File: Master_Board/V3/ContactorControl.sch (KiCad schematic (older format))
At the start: 28 parts, among them J701 649002227222, J702 649004227222, J703 649004227222, J704 649004227222, Q701 BC849BLT1G, Q702 BC849BLT1G, Q703 BC849BLT1G, Q704 BC849BLT1G

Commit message: Rooting Master V3
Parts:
- removed J701: 649002227222, Connectors:649002227222, symbol 649002227222
- removed R705, R706, R707, R708: RC0805FR-071K1L, Resistors:R0805, symbol RC0805FR-071K1L
- removed R?: RC0805JR-076K8L, Resistors:R0805, symbol RC0805JR-076K8L
- removed U?: CPC1117NTR, IC:4-SOP, symbol CPC1117NTR
- added J704: 649002227222, Connectors:649002227222, symbol 649002227222
- added R705, R706, R707, R708: RC0805JR-072K2L, Resistors:R0805, symbol RC0805JR-072K2L
- added R712: RC0805JR-076K8L, Resistors:R0805, symbol RC0805JR-076K8L
- added U701: CPC1117NTR, IC:4-SOP, symbol CPC1117NTR
- renumbered J702 to J701, J703 to J702, J704 to J703
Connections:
- net 12V_Contactor: now also J704.2; no longer RL701.7, RL701.8
- net 3.3V: now also U701.4 (DC+)
- net DGND: now also R712.2
- net Kill_Switch_State: now also U701.3 (DC-)
- net at Q701.3 (C): now also R705.1
- net at RL701.3: now also R705.2
- net at RL702.3: now also R706.2
- net at RL703.3: now also R707.2
- net at RL704.3: now also R708.2
- net at Q702.3 (C): now also R706.1
- net at Q703.3 (C): now also R707.1
- net at Q704.3 (C): now also R708.1
- new net: R712.1, U701.2 (C-)
- new net 12V_Protected: J704.1, RL701.7, RL701.8, U701.1 (A+)
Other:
- note removed: "Bouton d'arrêt d'urgence"
- moved on the sheet: D701, D702, D703, J701, J702, J703, Q701, Q702, Q703, Q704, R701, R702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

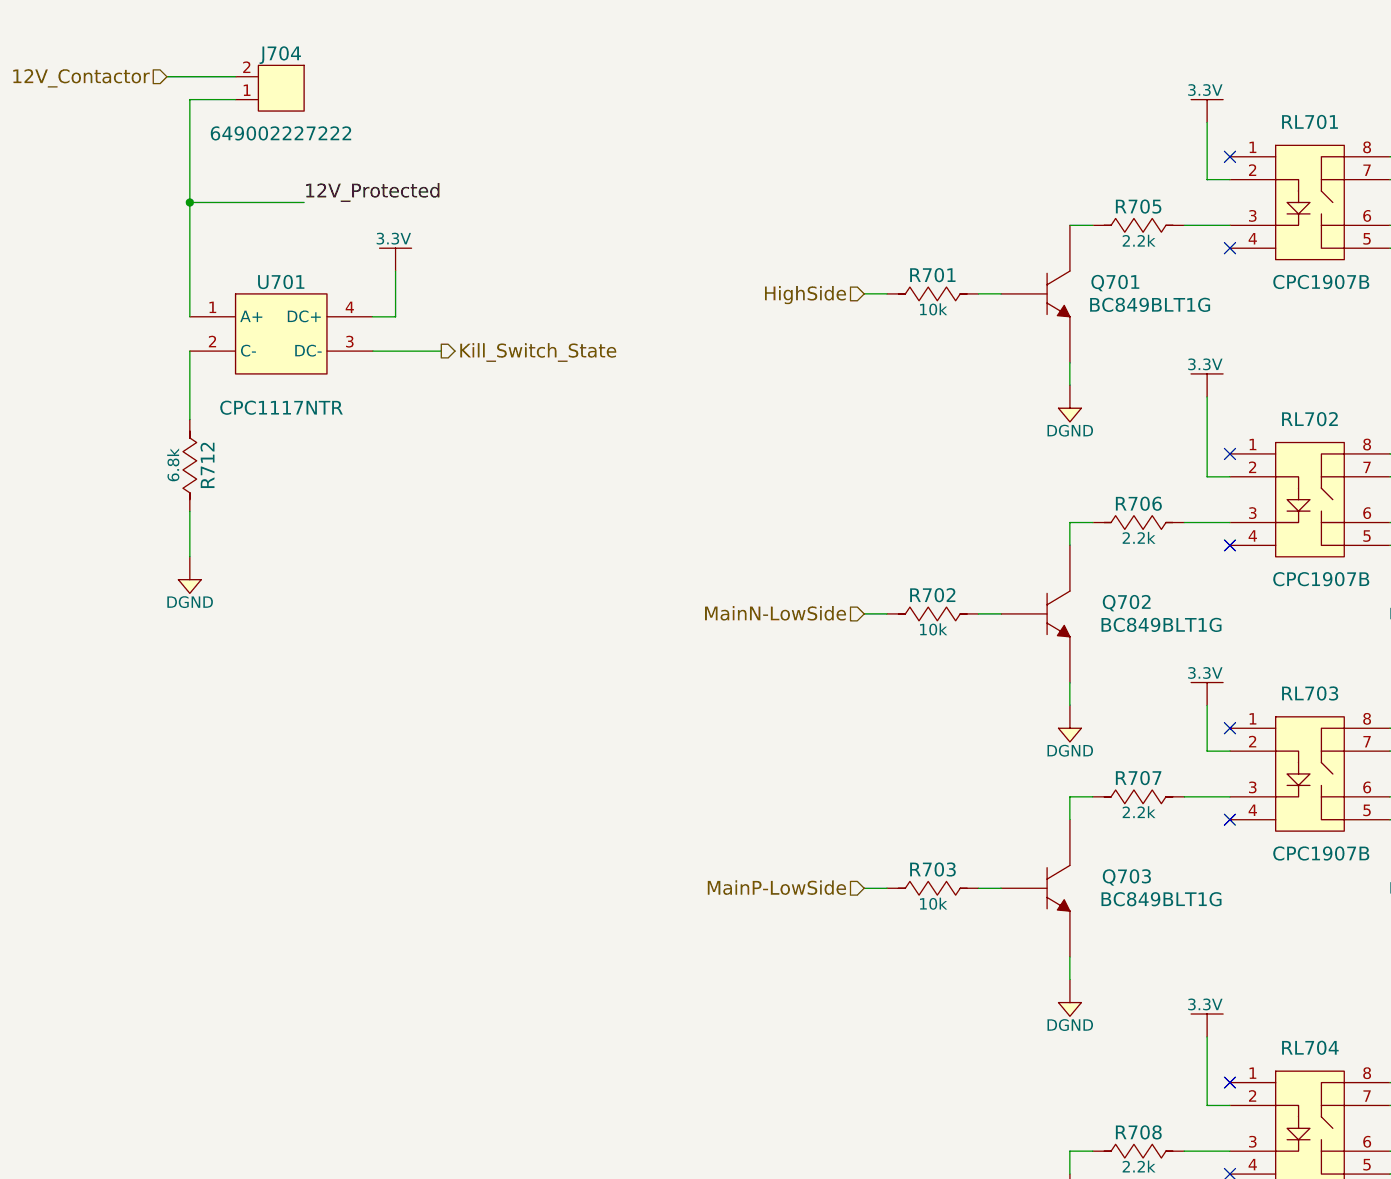
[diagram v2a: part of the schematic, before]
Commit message: Correction of kill switch circuit
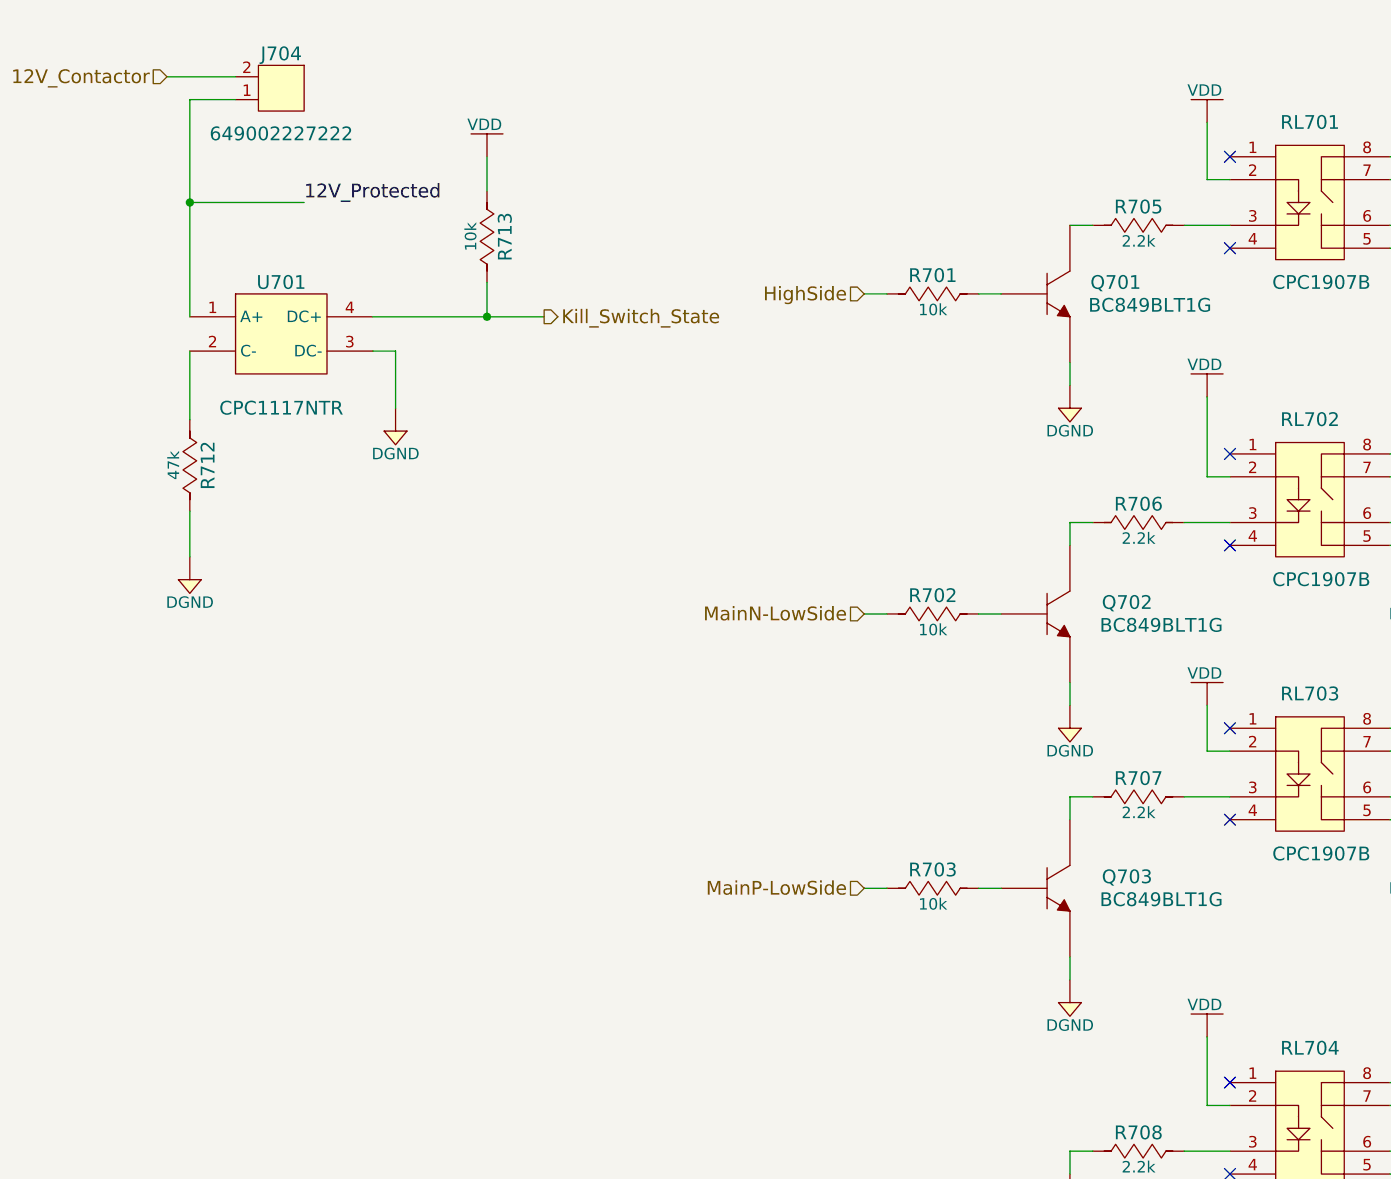
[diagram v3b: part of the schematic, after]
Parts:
- removed R712: RC0805JR-076K8L, Resistors:R0805, symbol RC0805JR-076K8L
- added R712: RC0805JR-0747KL, Resistors:R0805, symbol RC0805JR-0747KL
- added R713: RC0805JR-0710KL, Resistors:R0805, symbol RC0805JR-0710KL
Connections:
- net DGND: now also U701.3 (DC-), R712.2
- net Kill_Switch_State: now also U701.4 (DC+), R713.2; no longer U701.3 (DC-)
- net at U701.2 (C-): now also R712.1
- net 3.3V renamed VDD
- net VDD: now also R713.1; no longer U701.4 (DC+)
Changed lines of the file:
@@
-$EndComp
-$Comp
-L 3.3V #PWR073
-U 1 1 59467AF2
-P 5950 1150
-F 0 "#PWR073" H 5950 1000 50  0001 C CNN
-F 1 "3.3V" H 5940 1290 50  0000 C CNN
-F 2 "" H 5950 1150 60  0000 C CNN
-F 3 "" H 5950 1150 60  0000 C CNN
-	1    5950 1150
-	1    0    0    -1
 $EndComp
 $Comp
@@
 	1    0    0    -1
 $EndComp
-$Comp
-L 3.3V #PWR074
-U 1 1 59467F7E
-P 5950 2350
-F 0 "#PWR074" H 5950 2200 50  0001 C CNN
-F 1 "3.3V" H 5940 2490 50  0000 C CNN
-F 2 "" H 5950 2350 60  0000 C CNN
-F 3 "" H 5950 2350 60  0000 C CNN
-	1    5950 2350
-	1    0    0    -1
-$EndComp
 Wire Wire Line
 	9100 1700 9300 1700
@@
 	1    0    0    -1
 $EndComp
-$Comp
-L 3.3V #PWR075
-U 1 1 5946A659
-P 5950 5150
-F 0 "#PWR075" H 5950 5000 50  0001 C CNN
-F 1 "3.3V" H 5940 5290 50  0000 C CNN
-F 2 "" H 5950 5150 60  0000 C CNN
-F 3 "" H 5950 5150 60  0000 C CNN
-	1    5950 5150
-	1    0    0    -1
-$EndComp
 Wire Wire Line
 	4950 6050 5050 6050
@@
 	5350 5750 5350 5650
 $Comp
-L DGND #PWR076
+L DGND #PWR073
 U 1 1 594D7DB4
 P 5350 6500
-F 0 "#PWR076" H 5350 6330 50  0001 C CNN
+F 0 "#PWR073" H 5350 6330 50  0001 C CNN
 F 1 "DGND" H 5350 6400 50  0000 C CNN
 F 2 "" H 5350 6600 60  0000 C CNN
@@
 	5350 4100 5350 4200
 $Comp
-L DGND #PWR077
+L DGND #PWR074
 U 1 1 594D9A79
 P 5350 5000
-F 0 "#PWR077" H 5350 4830 50  0001 C CNN
+F 0 "#PWR074" H 5350 4830 50  0001 C CNN
 F 1 "DGND" H 5350 4900 50  0000 C CNN
 F 2 "" H 5350 5100 60  0000 C CNN
@@
 	5350 2900 5350 3000
 $Comp
-L DGND #PWR078
+L DGND #PWR075
 U 1 1 594DA7ED
 P 5350 3800
-F 0 "#PWR078" H 5350 3630 50  0001 C CNN
+F 0 "#PWR075" H 5350 3630 50  0001 C CNN
 F 1 "DGND" H 5350 3700 50  0000 C CNN
 F 2 "" H 5350 3900 60  0000 C CNN
@@
 	5450 1600 5350 1600
 $Comp
-L DGND #PWR079
+L DGND #PWR076
 U 1 1 594DC6F0
 P 5350 2400
-F 0 "#PWR079" H 5350 2230 50  0001 C CNN
+F 0 "#PWR076" H 5350 2230 50  0001 C CNN
 F 1 "DGND" H 5350 2300 50  0000 C CNN
 F 2 "" H 5350 2500 60  0000 C CNN
@@
 Text Notes 8500 800  0    60   ~ 0
 Note: Short female connector's pin 2 & 4 for interlock status.
-$Comp
-L 3.3V #PWR080
-U 1 1 595D7BC2
-P 5950 3700
-F 0 "#PWR080" H 5950 3550 50  0001 C CNN
-F 1 "3.3V" H 5940 3840 50  0000 C CNN
-F 2 "" H 5950 3700 60  0000 C CNN
-F 3 "" H 5950 3700 60  0000 C CNN
-	1    5950 3700
-	1    0    0    -1
-$EndComp
 Wire Wire Line
 	6050 3900 5950 3900
@@
 Text Label 2000 1500 0    60   ~ 0
 12V_Protected
-$Comp
-L 3.3V #PWR081
-U 1 1 5A88D05E
-P 2400 1800
-F 0 "#PWR081" H 2400 1650 50  0001 C CNN
-F 1 "3.3V" H 2390 1940 50  0000 C CNN
-F 2 "" H 2400 1800 60  0000 C CNN
-F 3 "" H 2400 1800 60  0000 C CNN
-	1    2400 1800
-	1    0    0    -1
-$EndComp
-Wire Wire Line
-	2300 2000 2400 2000
-Wire Wire Line
-	2400 2000 2400 1800
-$Comp
-L RC0805JR-076K8L R712
-U 1 1 5A88D1B7
+Wire Wire Line
+	1500 2150 1500 2450
+$Comp
+L DGND #PWR077
+U 1 1 5A88D5BF
+P 1500 3150
+F 0 "#PWR077" H 1500 2980 50  0001 C CNN
+F 1 "DGND" H 1500 3050 50  0000 C CNN
+F 2 "" H 1500 3250 60  0000 C CNN
+F 3 "" H 1480 3060 60  0000 C CNN
+	1    1500 3150
+	1    0    0    -1
+$EndComp
+Wire Wire Line
+	1500 2850 1500 3050
+Text HLabel 3050 2000 2    60   Output ~ 0
+Kill_Switch_State
+Wire Wire Line
+	6850 1400 6850 1300
+Text Label 7050 1300 0    60   ~ 0
+12V_Protected
+Wire Wire Line
+	2300 2000 3050 2000
+$Comp
+L DGND #PWR078
+U 1 1 5A90F0FC
+P 2400 2500
+F 0 "#PWR078" H 2400 2330 50  0001 C CNN
+F 1 "DGND" H 2400 2400 50  0000 C CNN
+F 2 "" H 2400 2600 60  0000 C CNN
+F 3 "" H 2380 2410 60  0000 C CNN
+	1    2400 2500
+	1    0    0    -1
+$EndComp
+Wire Wire Line
+	2300 2150 2400 2150
+Wire Wire Line
+	2400 2150 2400 2400
+$Comp
+L RC0805JR-0710KL R713
+U 1 1 5A90F994
+P 2800 1650
+F 0 "R713" H 2800 1730 60  0000 C CNN
+F 1 "RC0805JR-0710KL" H 2800 1350 50  0001 C CNN
+F 2 "Resistors:R0805" H 2800 750 30  0001 C CNN
+F 3 "http://www.yageo.com/documents/recent/PYu-RC_Group_51_RoHS_L_7.pdf" H 2800 700 30  0001 C CNN
+F 4 "Digikey" H 2800 1250 60  0001 C CNN "Supplier"
+F 5 "311-10KARCT-ND" H 2800 1150 60  0001 C CNN "Supplier Part Number"
+F 6 "Yageo" H 2800 1050 60  0001 C CNN "Manufacturer"
+F 7 "RC0805JR-0710KL" H 2800 950 60  0001 C CNN "Manufacturer Part Number"
+F 8 "RES SMD 10K OHM 5% 1/8W 0805" H 2800 850 60  0001 C CNN "Description"
+F 9 "10k" H 2800 1580 50  0000 C CNN "Resistance (Ohms)"
+F 10 "±5%" H 3210 1570 50  0001 C CNN "Tolerance (%)"
+F 11 "1/8W" H 2800 1510 50  0001 C CNN "Puissance (Watts)"
+	1    2800 1650
+	0    1    1    0
+$EndComp
+Wire Wire Line
+	2800 1300 2800 1450
+Wire Wire Line
+	2800 1850 2800 2000
+Connection ~ 2800 2000
+$Comp
+L RC0805JR-0747KL R712
+U 1 1 5A91B603
 P 1500 2650
 F 0 "R712" H 1500 2730 60  0000 C CNN
-F 1 "RC0805JR-076K8L" H 1500 2350 50  0001 C CNN
+F 1 "RC0805JR-0747KL" H 1500 2350 50  0001 C CNN
 F 2 "Resistors:R0805" H 1500 1750 30  0001 C CNN
 F 3 "http://www.yageo.com/documents/recent/PYu-RC_Group_51_RoHS_L_7.pdf" H 1500 1700 30  0001 C CNN
 F 4 "Digikey" H 1500 2250 60  0001 C CNN "Supplier"
-F 5 "311-6.8KARCT-ND" H 1500 2150 60  0001 C CNN "Supplier Part Number"
+F 5 "311-47KARCT-ND" H 1500 2150 60  0001 C CNN "Supplier Part Number"
 F 6 "Yageo" H 1500 2050 60  0001 C CNN "Manufacturer"
-F 7 "RC0805JR-076K8L" H 1500 1950 60  0001 C CNN "Manufacturer Part Number"
-F 8 "RES SMD 6.8K OHM 5% 1/8W 0805" H 1500 1850 60  0001 C CNN "Description"
-F 9 "6.8k" H 1500 2580 50  0000 C CNN "Resistance (Ohms)"
+F 7 "RC0805JR-0747KL" H 1500 1950 60  0001 C CNN "Manufacturer Part Number"
+F 8 "RES SMD 47K OHM 5% 1/8W 0805" H 1500 1850 60  0001 C CNN "Description"
+F 9 "47k" H 1500 2580 50  0000 C CNN "Resistance (Ohms)"
 F 10 "±5%" H 1910 2570 50  0001 C CNN "Tolerance (%)"
 F 11 "1/8W" H 1500 2510 50  0001 C CNN "Puissance (Watts)"
@@
 	0    1    1    0
 $EndComp
-Wire Wire Line
-	1500 2150 1500 2450
-$Comp
-L DGND #PWR082
-U 1 1 5A88D5BF
-P 1500 3150
-F 0 "#PWR082" H 1500 2980 50  0001 C CNN
-F 1 "DGND" H 1500 3050 50  0000 C CNN
-F 2 "" H 1500 3250 60  0000 C CNN
-F 3 "" H 1480 3060 60  0000 C CNN
-	1    1500 3150
-	1    0    0    -1
-$EndComp
-Wire Wire Line
-	1500 2850 1500 3050
-Text HLabel 2600 2150 2    60   Output ~ 0
-Kill_Switch_State
-Wire Wire Line
-	2300 2150 2600 2150
-Wire Wire Line
-	6850 1400 6850 1300
-Text Label 7050 1300 0    60   ~ 0
-12V_Protected
+$Comp
+L VDD #PWR079
+U 1 1 5A91C8A8
+P 2800 1300
+F 0 "#PWR079" H 2800 1150 50  0001 C CNN
+F 1 "VDD" H 2790 1440 50  0000 C CNN
+F 2 "" H 2800 1300 60  0000 C CNN
+F 3 "" H 2800 1150 60  0000 C CNN
+	1    2800 1300
+	1    0    0    -1
+$EndComp
+$Comp
+L VDD #PWR080
+U 1 1 5A91C8F6
+P 5950 1150
+F 0 "#PWR080" H 5950 1000 50  0001 C CNN
+F 1 "VDD" H 5940 1290 50  0000 C CNN
+F 2 "" H 5950 1150 60  0000 C CNN
+F 3 "" H 5950 1000 60  0000 C CNN
+	1    5950 1150
+	1    0    0    -1
+$EndComp
+$Comp
+L VDD #PWR081
+U 1 1 5A91C944
+P 5950 2350
+F 0 "#PWR081" H 5950 2200 50  0001 C CNN
+F 1 "VDD" H 5940 2490 50  0000 C CNN
+F 2 "" H 5950 2350 60  0000 C CNN
+F 3 "" H 5950 2200 60  0000 C CNN
+	1    5950 2350
+	1    0    0    -1
+$EndComp
+$Comp
+L VDD #PWR082
+U 1 1 5A91C992
+P 5950 3700
+F 0 "#PWR082" H 5950 3550 50  0001 C CNN
+F 1 "VDD" H 5940 3840 50  0000 C CNN
+F 2 "" H 5950 3700 60  0000 C CNN
+F 3 "" H 5950 3550 60  0000 C CNN
+	1    5950 3700
+	1    0    0    -1
+$EndComp
+$Comp
+L VDD #PWR083
+U 1 1 5A91C9E0
+P 5950 5150
+F 0 "#PWR083" H 5950 5000 50  0001 C CNN
+F 1 "VDD" H 5940 5290 50  0000 C CNN
+F 2 "" H 5950 5150 60  0000 C CNN
+F 3 "" H 5950 5000 60  0000 C CNN
+	1    5950 5150
+	1    0    0    -1
+$EndComp
 $EndSCHEMATC
